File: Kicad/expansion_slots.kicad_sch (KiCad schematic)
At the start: 32 parts, among them J901 Conn_01x06, J902 Neotron-Expansion-Slot, J903 Neotron-Expansion-Slot, J904 Neotron-Expansion-Slot, J905 Neotron-Expansion-Slot, J906 Conn_01x09, J907 Conn_01x09, J908 Conn_01x09

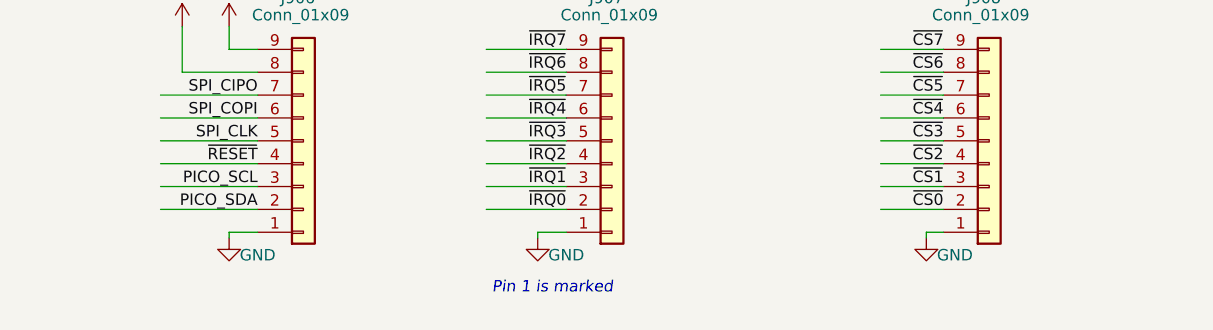
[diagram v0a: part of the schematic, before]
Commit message: Set headers as DNF=0. We expect people to fit them.
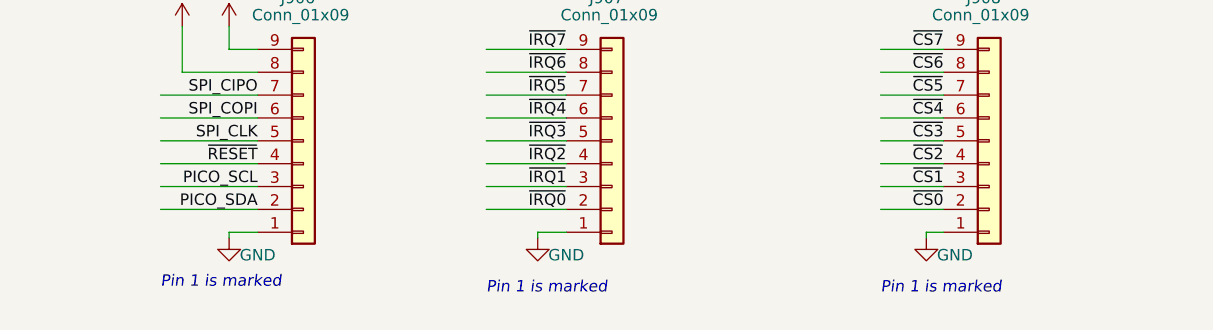
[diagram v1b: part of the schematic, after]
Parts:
- J901: DNP 1 -> 0
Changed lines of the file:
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@@
     (effects (font (size 1.27 1.27)) (justify left bottom))
+  )
+  (text "Pin 1 is marked" (at 106.68 195.58 0)
+    (effects (font (size 1.27 1.27) italic) (justify left bottom))
   )
   (text "Slot 2" (at 13.335 76.2 0)
@@
     (effects (font (size 2.54 2.54)) (justify left bottom))
   )
-  (text "Pin 1 is marked" (at 63.5 195.58 0)
+  (text "Pin 1 is marked" (at 62.865 195.58 0)
     (effects (font (size 1.27 1.27) italic) (justify left bottom))
   )
@@
   (text "Test Headers" (at 13.335 158.75 0)
     (effects (font (size 2.54 2.54)) (justify left bottom))
+  )
+  (text "Pin 1 is marked" (at 26.67 194.945 0)
+    (effects (font (size 1.27 1.27) italic) (justify left bottom))
   )
   (text "Inputs/Outputs" (at 13.335 17.145 0)
@@
       (effects (font (size 1.27 1.27)) hide)
     )
-    (property "DNP" "1" (id 4) (at 177.8 43.815 0)
-      (effects (font (size 1.27 1.27)) hide)
-    )
+    (property "DNP" "0" (id 4) (at 177.8 43.815 0)
+      (effects (font (size 1.27 1.27)) hide)
+    )
